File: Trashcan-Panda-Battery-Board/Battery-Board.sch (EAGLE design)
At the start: 5 parts, among them J1 B2B-PH-SM4-TB(LF)(SN)

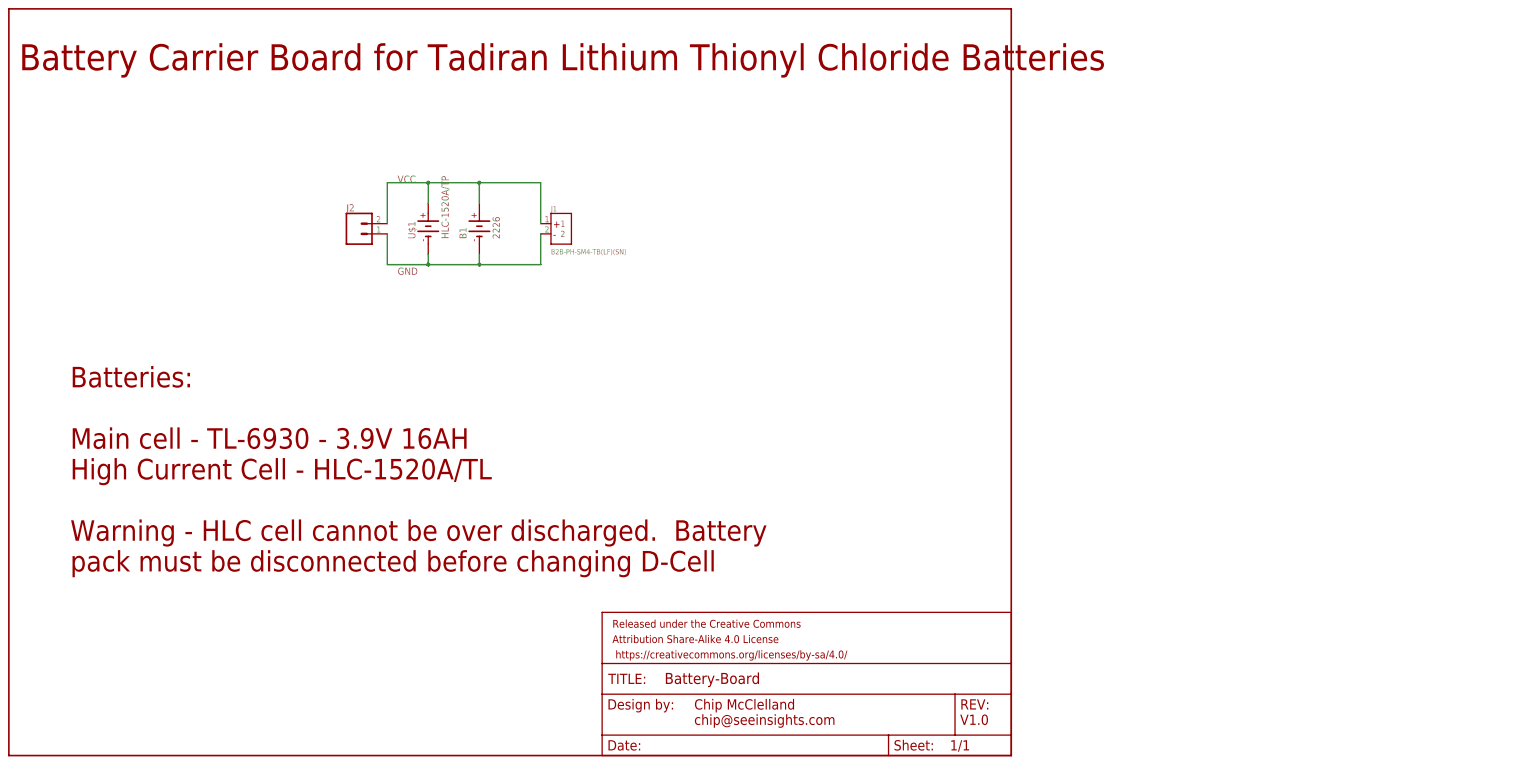
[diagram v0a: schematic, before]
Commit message: Updated battery board to v1.1
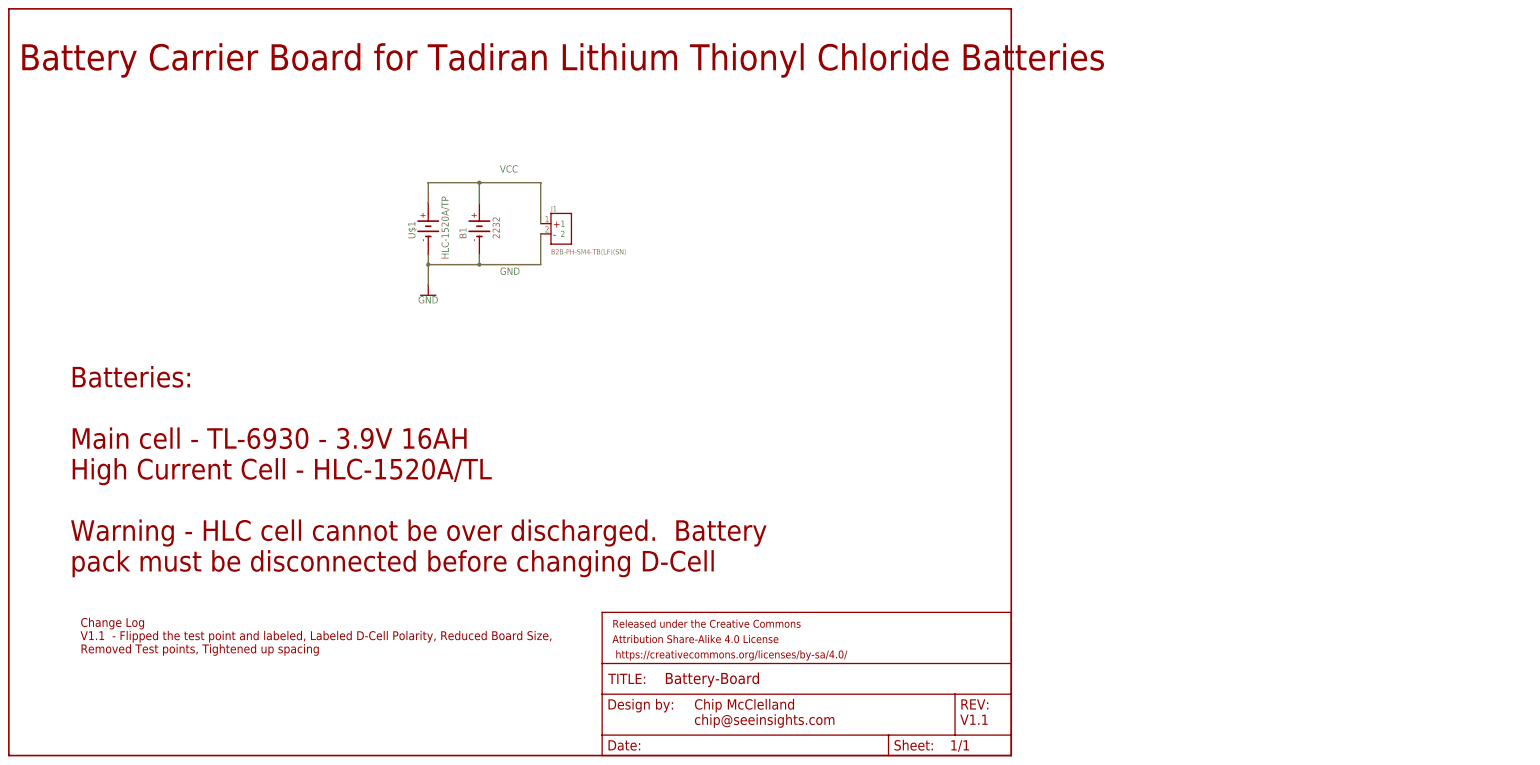
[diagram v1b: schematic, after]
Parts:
- removed J2: (no value), SparkFun-Connectors:CONN_02
- B1: value 2226 -> 2232; device Battery-Board:2226 -> Battery-Board:2232
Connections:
- net GND: no longer J2.1
- net VCC: no longer J2.2
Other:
- note added: "Change Log V1.1 - Flipped the test point and labeled, Labeled D-Cell Polarity, Reduced Board Size, Removed Test points, Tightened up spacing"
- note added: "V1.1"
- note removed: "V1.0"
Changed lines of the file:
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@@
 </classes>
 <parts>
-<part name="B1" library="Battery-Board" deviceset="2226" device="" override_package3d_urn="urn:adsk.eagle:package:34202687/3" override_package_urn="urn:adsk.eagle:footprint:34202688/1" override_locally_modified="yes"/>
+<part name="B1" library="Battery-Board" deviceset="2232" device="" override_package3d_urn="urn:adsk.eagle:package:34202687/3" override_package_urn="urn:adsk.eagle:footprint:34202688/1" override_locally_modified="yes"/>
 <part name="J1" library="Custom Components" deviceset="B2B-PH-SM4-TB(LF)(SN)" device=""/>
-<part name="J2" library="SparkFun-Connectors" library_urn="urn:adsk.eagle:library:513" deviceset="CONN_02" device="" package3d_urn="urn:adsk.eagle:package:38039/1"/>
 <part name="U$1" library="Battery-Board" deviceset="HLC-1520A/TP" device=""/>
 <part name="FRAME1" library="SparkFun-Aesthetics" library_urn="urn:adsk.eagle:library:507" deviceset="FRAME-LETTER" device="" package3d_urn="urn:adsk.eagle:package:37121/1"/>
+<part name="GND1" library="SparkFun-PowerSymbols" library_urn="urn:adsk.eagle:library:530" deviceset="GND" device=""/>
 </parts>
 <sheets>
@@
 <text x="170.18" y="7.62" size="2.54" layer="94">Chip McClelland
 chip@seeinsights.com</text>
-<text x="236.22" y="7.62" size="2.54" layer="94">V1.0</text>
+<text x="236.22" y="7.62" size="2.54" layer="94">V1.1</text>
+<text x="17.78" y="25.4" size="2.1844" layer="94">Change Log
+V1.1  - Flipped the test point and labeled, Labeled D-Cell Polarity, Reduced Board Size,
+Removed Test points, Tightened up spacing</text>
 </plain>
 <instances>
@@
 <attribute name="VALUE" x="134.61901875" y="124.457059375" size="1.270490625" layer="96"/>
 </instance>
-<instance part="J2" gate="G$1" x="86.36" y="129.54" smashed="yes">
-<attribute name="VALUE" x="83.82" y="124.714" size="1.778" layer="96" font="vector"/>
-<attribute name="NAME" x="83.82" y="135.128" size="1.778" layer="95" font="vector"/>
-</instance>
 <instance part="U$1" gate="G$1" x="104.14" y="129.54" smashed="yes" rot="R90">
 <attribute name="NAME" x="100.961490625" y="128.2686" size="1.77996875" layer="95" rot="R90"/>
-<attribute name="VALUE" x="109.2233" y="128.26916875" size="1.779159375" layer="96" rot="R90"/>
+<attribute name="VALUE" x="109.2233" y="123.18916875" size="1.779159375" layer="96" rot="R90"/>
 </instance>
 <instance part="FRAME1" gate="G$1" x="0" y="0" smashed="yes"/>
@@
 <attribute name="DRAWING_NAME" x="162.814" y="17.78" size="2.7432" layer="94" font="vector"/>
 </instance>
+<instance part="GND1" gate="1" x="104.14" y="114.3" smashed="yes">
+<attribute name="VALUE" x="104.14" y="114.046" size="1.778" layer="96" align="top-center"/>
+</instance>
 </instances>
 <busses>
@@
 <net name="GND" class="0">
 <segment>
-<pinref part="J2" gate="G$1" pin="1"/>
-<wire x1="93.98" y1="129.54" x2="93.98" y2="121.92" width="0.1524" layer="91"/>
 <pinref part="J1" gate="G$1" pin="2"/>
-<wire x1="93.98" y1="121.92" x2="104.14" y2="121.92" width="0.1524" layer="91"/>
 <wire x1="104.14" y1="121.92" x2="116.84" y2="121.92" width="0.1524" layer="91"/>
 <wire x1="116.84" y1="121.92" x2="132.08" y2="121.92" width="0.1524" layer="91"/>
@@
 <pinref part="U$1" gate="G$1" pin="-"/>
 <wire x1="104.14" y1="124.46" x2="104.14" y2="121.92" width="0.1524" layer="91"/>
-<junction x="104.14" y="121.92"/>
 <pinref part="B1" gate="G$1" pin="-"/>
 <wire x1="116.84" y1="124.46" x2="116.84" y2="121.92" width="0.1524" layer="91"/>
 <junction x="116.84" y="121.92"/>
-<label x="96.52" y="119.38" size="1.778" layer="95"/>
+<label x="121.92" y="119.38" size="1.778" layer="95"/>
+<pinref part="GND1" gate="1" pin="GND"/>
+<wire x1="104.14" y1="121.92" x2="104.14" y2="116.84" width="0.1524" layer="91"/>
+<junction x="104.14" y="121.92"/>
 </segment>
 </net>
 <net name="VCC" class="0">
 <segment>
-<pinref part="J2" gate="G$1" pin="2"/>
-<wire x1="93.98" y1="132.08" x2="93.98" y2="142.24" width="0.1524" layer="91"/>
-<wire x1="93.98" y1="142.24" x2="104.14" y2="142.24" width="0.1524" layer="91"/>
 <pinref part="J1" gate="G$1" pin="1"/>
 <wire x1="104.14" y1="142.24" x2="116.84" y2="142.24" width="0.1524" layer="91"/>
@@
 <pinref part="U$1" gate="G$1" pin="+"/>
 <wire x1="104.14" y1="137.16" x2="104.14" y2="142.24" width="0.1524" layer="91"/>
-<junction x="104.14" y="142.24"/>
 <pinref part="B1" gate="G$1" pin="+"/>
 <wire x1="116.84" y1="137.16" x2="116.84" y2="142.24" width="0.1524" layer="91"/>
 <junction x="116.84" y="142.24"/>
-<label x="96.52" y="142.24" size="1.778" layer="95"/>
+<label x="121.92" y="144.78" size="1.778" layer="95"/>
 </segment>
 </net>

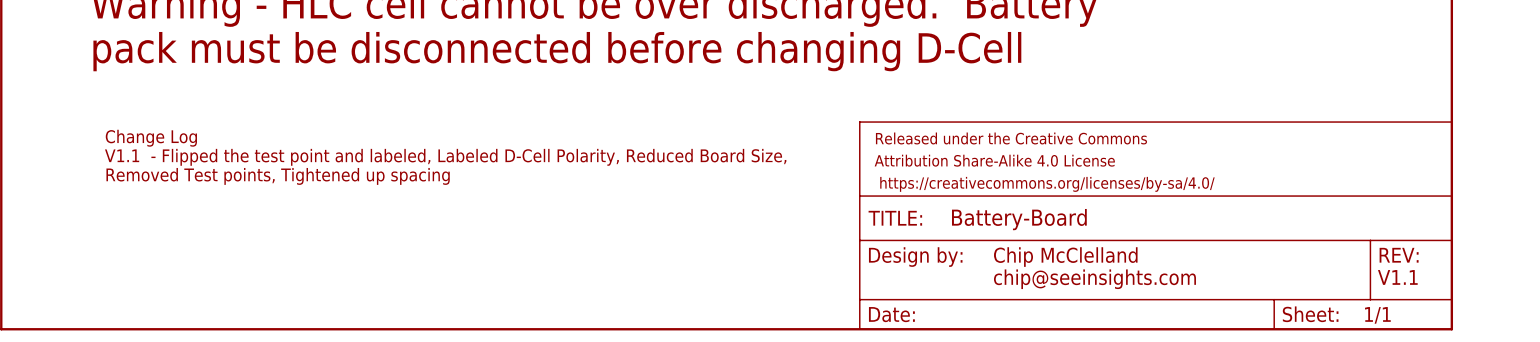
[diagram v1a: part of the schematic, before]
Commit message: Changed Battery Board Profile
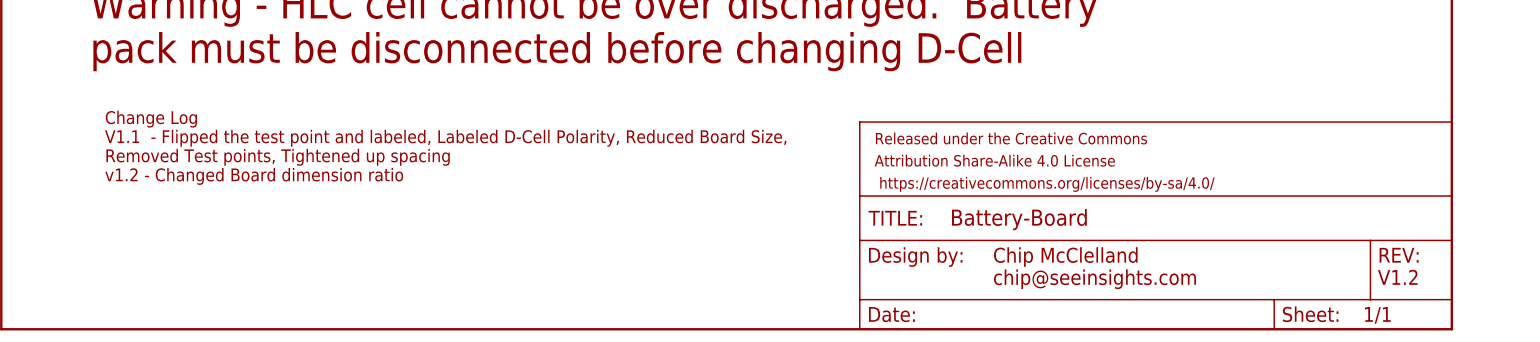
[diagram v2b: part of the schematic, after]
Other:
- note added: "Change Log V1.1 - Flipped the test point and labeled, Labeled D-Cell Polarity, Reduced Board Size, Removed Test points, Tightened up spacing v1.2 - Changed Board dimension ratio"
- note added: "V1.2"
- note removed: "Change Log V1.1 - Flipped the test point and labeled, Labeled D-Cell Polarity, Reduced Board Size, Removed Test points, Tightened up spacing"
- note removed: "V1.1"
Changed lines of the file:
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@@
 <text x="170.18" y="7.62" size="2.54" layer="94">Chip McClelland
 chip@seeinsights.com</text>
-<text x="236.22" y="7.62" size="2.54" layer="94">V1.1</text>
+<text x="236.22" y="7.62" size="2.54" layer="94">V1.2</text>
 <text x="17.78" y="25.4" size="2.1844" layer="94">Change Log
 V1.1  - Flipped the test point and labeled, Labeled D-Cell Polarity, Reduced Board Size,
-Removed Test points, Tightened up spacing</text>
+Removed Test points, Tightened up spacing
+v1.2 - Changed Board dimension ratio</text>
 </plain>
 <instances>
